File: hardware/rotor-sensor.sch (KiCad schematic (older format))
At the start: 26 parts, among them J1 Conn_01x03, J2 Conn_01x03, J3 Conn_01x03, U1 ATtiny202-SS, U2 EE-SX1081, U3 SM351LT

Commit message: Second hardware iteration (#3)
Cleaned up the schematic and reworked the entire PCB.
Replaced EE-SX1083 with EE-SX199, added 3D model and new component.
Added modified worksheet so that the PCB origin can be 0, 0.
Added scripts to execute certain tasks locally and updated the workflow accordingly.
Workflow now runs for the different variants.
The KiBot configuration has been merged into a single file.
*Increased clearance between Slot sensor and PCB edge
Assigned component values to remaining components.
Connectors will now only be placed in the DEBUG variant
Rotated input filter capacitor for better ground connection
Adds panelization and panel configuration
Adds fiducials to board and added tab annotation as a footprint.
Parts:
- removed TP1, TP2, TP3, TP4, TP5, TP6: TestPoint_Alt, TestPoint:TestPoint_Pad_D1.0mm, symbol Connector:TestPoint_Alt
- removed U2: EE-SX1081, local:EE-SX1081, symbol local:EE-SX1081
- added FID1, FID2: Fiducial, Fiducial:Fiducial_0.5mm_Mask1.5mm, symbol Mechanical:Fiducial
- added TP1: +, TestPoint:TestPoint_Pad_D1.0mm, symbol Connector:TestPoint_Small
- added TP10: AC-, TestPoint:TestPoint_Pad_D1.0mm, symbol Connector:TestPoint_Small
- added TP11: AC+, TestPoint:TestPoint_Pad_D1.0mm, symbol Connector:TestPoint_Small
- added TP12: IN, TestPoint:TestPoint_Pad_D1.0mm, symbol Connector:TestPoint_Small
- added TP13: OUT, TestPoint:TestPoint_Pad_D1.0mm, symbol Connector:TestPoint_Small
- added TP2: COMA, TestPoint:TestPoint_Pad_D1.0mm, symbol Connector:TestPoint_Small
- added TP3: VD, TestPoint:TestPoint_Pad_D1.0mm, symbol Connector:TestPoint_Small
- added TP4: VCC, TestPoint:TestPoint_Pad_D1.0mm, symbol Connector:TestPoint_Small
- added TP5: -, TestPoint:TestPoint_Pad_D1.0mm, symbol Connector:TestPoint_Small
- added TP6: UPDI, TestPoint:TestPoint_Pad_D1.0mm, symbol Connector:TestPoint_Small
- added TP7: COMB, TestPoint:TestPoint_Pad_D1.0mm, symbol Connector:TestPoint_Small
- added TP8: W2, TestPoint:TestPoint_Pad_D1.0mm, symbol Connector:TestPoint_Small
- added TP9: SENSE, TestPoint:TestPoint_Pad_D1.0mm, symbol Connector:TestPoint_Small
- added U2: EE-SX199, local:EE-SX199, symbol local:EE-SX199
- C1, C2, C3: value C -> 100n
- J1, J2, J3: Config (none) -> +DEBUG
- L1: value L -> 10uH
- R1, R4, R5: value R -> 50m
- R2: value R -> 1k
- R3: value R -> 100
- R6, R7: value R -> 1k; Config (none) -> +IREF
- U3: Config (none) -> +HALL
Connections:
- net labels added: OS_INPUT, OS_OUTPUT, PA0_UPDI
- wire segments 60 -> 68
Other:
- note added: "EXTERNAL SENSOR\nCONNECTOR"
- note added: "EXTERNAL VOLTAGE\nREFERENCE"
- note added: "ONBOARD\nHALL SENSOR"
- note added: "ONBOARD\nOPTICAL SENSOR"
- note added: "VARIANT=EXTERNAL"
- note added: "VARIANT=HALL"
- note added: "VARIANT=IREF"
- note added: "VARIANT=OPTICAL"
- note removed: "ONBOARD PERIPHERALS"
- moved on the sheet: C1, C2, C3, D1, D2, D3, J1, J2, J3, L1, R1, R2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

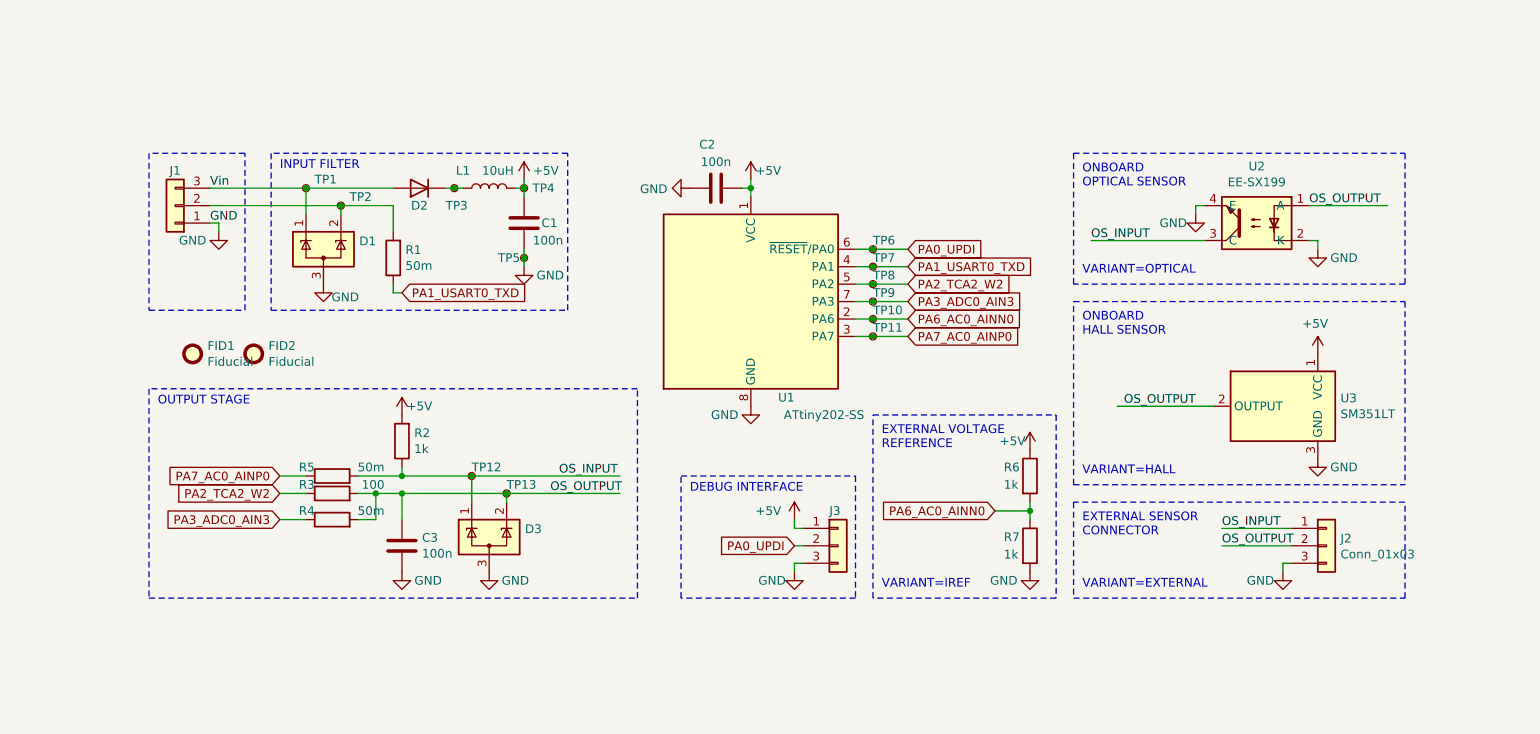
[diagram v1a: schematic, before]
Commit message: Adds LIN Transceiver to the design
Updates layout and schematic
Adds overcurrent protection IC and removes sense line
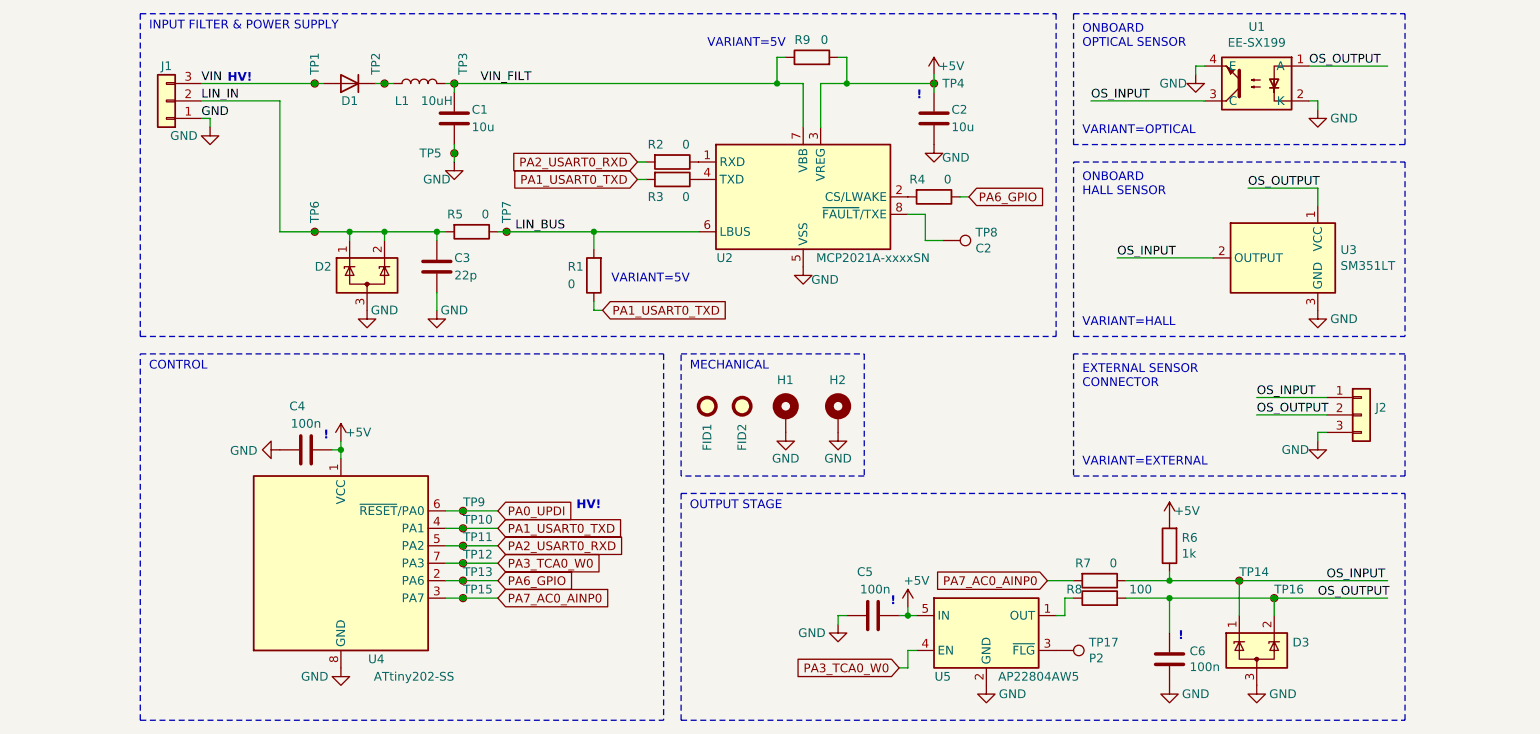
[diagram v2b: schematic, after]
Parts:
- removed J3: Conn_01x03, Connector_PinHeader_1.27mm:PinHeader_1x03_P1.27mm_Vertical, symbol Connector_Generic:Conn_01x03
- removed R5: 50m, Resistor_SMD:R_0603_1608Metric, symbol Device:R
- removed R6: 1k, Resistor_SMD:R_0603_1608Metric, symbol Device:R
- added C2: 10u, Capacitor_SMD:C_1206_3216Metric, symbol Device:C
- added C3: 22p, Capacitor_SMD:C_0603_1608Metric, symbol Device:C
- added C5: 100n, Capacitor_SMD:C_0603_1608Metric, symbol Device:C
- added H1, H2: MountingHole_Pad, MountingHole:MountingHole_2.2mm_M2_DIN965_Pad_TopOnly, symbol Mechanical:MountingHole_Pad
- added R1, R2, R3: 0, Resistor_SMD:R_0402_1005Metric, symbol Device:R
- added R9: 0, Resistor_SMD:R_0603_1608Metric, symbol Device:R
- added TP17: P2, TestPoint:TestPoint_Pad_D1.0mm, symbol Connector:TestPoint
- added TP4: V3, TestPoint:TestPoint_Pad_D1.0mm, symbol Connector:TestPoint_Small
- added TP7: C1, TestPoint:TestPoint_Pad_D1.0mm, symbol Connector:TestPoint_Small
- added TP8: C2, TestPoint:TestPoint_Pad_D1.0mm, symbol Connector:TestPoint
- added U2: MCP2021A-xxxxSN, Package_SO:SOIC-8_3.9x4.9mm_P1.27mm, symbol Interface_CAN_LIN:MCP2021A-xxxxSN
- added U5: AP22804AW5, Package_TO_SOT_SMD:SOT-23-5, symbol Power_Management:AP22804AW5
- C1: value 100n -> 10u; footprint Capacitor_SMD:C_0603_1608Metric -> Capacitor_SMD:C_1206_3216Metric
- J1: footprint Connector_PinHeader_2.54mm:PinHeader_1x03_P2.54mm_Vertical -> Connector_JST:JST_PH_B3B-PH-K_1x03_P2.00mm_Vertical
- R4: value 50m -> 0; footprint Resistor_SMD:R_0603_1608Metric -> Resistor_SMD:R_0402_1005Metric
- R5: renamed from R1; value 50m -> 0; footprint Resistor_SMD:R_0603_1608Metric -> Resistor_SMD:R_0402_1005Metric
- R7: value 1k -> 0; footprint Resistor_SMD:R_0603_1608Metric -> Resistor_SMD:R_0402_1005Metric; Config +IREF -> (none)
- TP1: value + -> V0
- TP10: renamed from TP7; value COMB -> M1
- TP11: renamed from TP8; value W2 -> M2
- TP12: renamed from TP9; value SENSE -> M3
- TP13: renamed from TP10; value AC- -> M6
- TP14: renamed from TP12; value IN -> P0
- TP15: renamed from TP11; value AC+ -> M7
- TP16: renamed from TP13; value OUT -> P1
- TP2: value COMA -> V1
- TP3: renamed from TP4; value VCC -> V2
- TP5: value - -> V4
- TP6: renamed from TP3; value VD -> C0
- TP9: renamed from TP6; value UPDI -> M0
- renumbered C2 to C4, C3 to C6, D2 to D1, D1 to D2, FID2 to FID1, FID1 to FID2, R2 to R6, R3 to R8, U2 to U1, U1 to U4
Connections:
- net labels added: LIN_BUS, LIN_IN, PA2_USART0_RXD, PA3_TCA0_W0, PA6_GPIO, VIN, VIN_FILT
- net labels removed: PA2_TCA2_W2, PA3_ADC0_AIN3, PA6_AC0_AINN0, Vin
- wire segments 68 -> 95
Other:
- note added: "!"
- note added: "CONTROL"
- note added: "HV!"
- note added: "INPUT FILTER & POWER SUPPLY"
- note added: "MECHANICAL"
- note added: "VARIANT=5V"
- note removed: "DEBUG INTERFACE"
- note removed: "EXTERNAL VOLTAGE\nREFERENCE"
- note removed: "INPUT FILTER"
- note removed: "VARIANT=IREF"
- moved on the sheet: C1, C4, C6, D1, D2, D3, FID1, FID2, J1, J2, L1, R5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

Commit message: Panelize?
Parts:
- added D4: LED_Small, LED_SMD:LED_0603_1608Metric, symbol Device:LED_Small
- added R10: 220, Resistor_SMD:R_0603_1608Metric, symbol Device:R
- R1, R9: Config (none) -> +5V
- U2: Config (none) -> -5V
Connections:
- wire segments 95 -> 100
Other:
- note added: "VARIANT=12V"
- moved on the sheet: C5, C6, D3, R7, R8, TP17, U5
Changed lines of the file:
@@
 L Device:R R8
 U 1 1 6122E61F
-P 7800 5100
-F 0 "R8" V 7850 5200 50  0000 L CNN
-F 1 "100" V 7850 4800 50  0000 L CNN
-F 2 "Resistor_SMD:R_0603_1608Metric" V 7730 5100 50  0001 C CNN
-F 3 "~" H 7800 5100 50  0001 C CNN
-	1    7800 5100
+P 7450 5100
+F 0 "R8" V 7500 5200 50  0000 L CNN
+F 1 "100" V 7500 4800 50  0000 L CNN
+F 2 "Resistor_SMD:R_0603_1608Metric" V 7380 5100 50  0001 C CNN
+F 3 "~" H 7450 5100 50  0001 C CNN
+	1    7450 5100
 	0    -1   -1   0
 $EndComp
@@
 	-1   0    0    1
 $EndComp
-Text GLabel 7500 5000 0    50   Input ~ 0
+Text GLabel 7150 5000 0    50   Input ~ 0
 PA7_AC0_AINP0
 Wire Wire Line
-	7600 5100 7650 5100
+	7250 5100 7300 5100
 Text GLabel 4350 4700 2    50   Input ~ 0
 PA1_USART0_TXD
@@
 L Power_Protection:SP0502BAHT D3
 U 1 1 613650DD
-P 8700 5400
-F 0 "D3" H 8905 5446 50  0000 L CNN
-F 1 "SP0502BAHT" H 8900 5350 50  0001 L CNN
-F 2 "Package_TO_SOT_SMD:SOT-23" H 8925 5350 50  0001 L CNN
-F 3 "http://www.littelfuse.com/~/media/files/littelfuse/technical%20resources/documents/data%20sheets/sp05xxba.pdf" H 8825 5525 50  0001 C CNN
-	1    8700 5400
+P 8700 5450
+F 0 "D3" H 8905 5496 50  0000 L CNN
+F 1 "SP0502BAHT" H 8900 5400 50  0001 L CNN
+F 2 "Package_TO_SOT_SMD:SOT-23" H 8925 5400 50  0001 L CNN
+F 3 "http://www.littelfuse.com/~/media/files/littelfuse/technical%20resources/documents/data%20sheets/sp05xxba.pdf" H 8825 5575 50  0001 C CNN
+	1    8700 5450
 	1    0    0    -1
 $EndComp
@@
 	8200 4950 8200 5000
 Wire Wire Line
-	8200 5300 8200 5100
+	8200 5350 8200 5100
 $Comp
 L power:GND #PWR024
 U 1 1 613B542D
-P 8700 5600
-F 0 "#PWR024" H 8700 5350 50  0001 C CNN
-F 1 "GND" H 8850 5550 50  0000 C CNN
-F 2 "" H 8700 5600 50  0001 C CNN
-F 3 "" H 8700 5600 50  0001 C CNN
-	1    8700 5600
+P 8700 5650
+F 0 "#PWR024" H 8700 5400 50  0001 C CNN
+F 1 "GND" H 8850 5600 50  0000 C CNN
+F 2 "" H 8700 5650 50  0001 C CNN
+F 3 "" H 8700 5650 50  0001 C CNN
+	1    8700 5650
 	1    0    0    -1
 $EndComp
@@
 L power:GND #PWR023
 U 1 1 6127F551
-P 8200 5600
-F 0 "#PWR023" H 8200 5350 50  0001 C CNN
-F 1 "GND" H 8350 5550 50  0000 C CNN
-F 2 "" H 8200 5600 50  0001 C CNN
-F 3 "" H 8200 5600 50  0001 C CNN
-	1    8200 5600
+P 8200 5650
+F 0 "#PWR023" H 8200 5400 50  0001 C CNN
+F 1 "GND" H 8350 5600 50  0000 C CNN
+F 2 "" H 8200 5650 50  0001 C CNN
+F 3 "" H 8200 5650 50  0001 C CNN
+	1    8200 5650
 	1    0    0    -1
 $EndComp
@@
 L Device:C C6
 U 1 1 61263E24
-P 8200 5450
-F 0 "C6" H 8315 5496 50  0000 L CNN
-F 1 "100n" H 8315 5405 50  0000 L CNN
-F 2 "Capacitor_SMD:C_0603_1608Metric" H 8238 5300 50  0001 C CNN
-F 3 "~" H 8200 5450 50  0001 C CNN
-	1    8200 5450
+P 8200 5500
+F 0 "C6" H 8315 5546 50  0000 L CNN
+F 1 "100n" H 8315 5455 50  0000 L CNN
+F 2 "Capacitor_SMD:C_0603_1608Metric" H 8238 5350 50  0001 C CNN
+F 3 "~" H 8200 5500 50  0001 C CNN
+	1    8200 5500
 	1    0    0    -1
 $EndComp
@@
 OUTPUT STAGE
 Wire Wire Line
-	8200 5000 7950 5000
-Wire Wire Line
-	7650 5000 7500 5000
+	8200 5000 7600 5000
+Wire Wire Line
+	7300 5000 7150 5000
 Text GLabel 4350 4600 2    50   Input ~ 0
 PA0_UPDI
@@
 	8350 2050 8400 2050
 Wire Wire Line
-	8800 5200 8800 5100
+	8800 5250 8800 5100
 Connection ~ 8800 5100
 Wire Wire Line
-	8600 5200 8600 5000
+	8600 5250 8600 5000
 Connection ~ 8600 5000
 Wire Wire Line
@@
 F 2 "Package_SO:SOIC-8_3.9x4.9mm_P1.27mm" H 6125 2875 50  0001 C CNN
 F 3 "http://ww1.microchip.com/downloads/en/DeviceDoc/20002298C.pdf" H 6125 2875 50  0001 C CNN
+F 4 "-5V" H 6100 2800 50  0001 C CNN "Config"
 	1    6100 2800
 	1    0    0    -1
@@
 Text GLabel 4350 4800 2    50   Input ~ 0
 PA2_USART0_RXD
-Wire Wire Line
-	7950 5100 8200 5100
 $Comp
 L Power_Management:AP22804AW5 U5
 U 1 1 623B800F
-P 7150 5300
-F 0 "U5" H 6900 5050 50  0000 C CNN
-F 1 "AP22804AW5" H 7450 5050 50  0000 C CNN
-F 2 "Package_TO_SOT_SMD:SOT-23-5" H 7150 4900 50  0001 C CNN
-F 3 "https://www.diodes.com/assets/Datasheets/AP22804_14.pdf" H 7150 5350 50  0001 C CNN
-	1    7150 5300
+P 6800 5300
+F 0 "U5" H 6550 5050 50  0000 C CNN
+F 1 "AP22804AW5" H 7100 5050 50  0000 C CNN
+F 2 "Package_TO_SOT_SMD:SOT-23-5" H 6800 4900 50  0001 C CNN
+F 3 "https://www.diodes.com/assets/Datasheets/AP22804_14.pdf" H 6800 5350 50  0001 C CNN
+	1    6800 5300
 	1    0    0    -1
 $EndComp
@@
 	5150 2700 5200 2700
 Wire Wire Line
-	7550 5200 7600 5200
-Wire Wire Line
-	7600 5200 7600 5100
+	7200 5200 7250 5200
+Wire Wire Line
+	7250 5200 7250 5100
 Text GLabel 4350 4900 2    50   Input ~ 0
 PA3_TCA0_W0
 Text GLabel 4350 5000 2    50   Input ~ 0
 PA6_GPIO
-Text GLabel 6650 5500 0    50   Input ~ 0
+Text GLabel 6300 5500 0    50   Input ~ 0
 PA3_TCA0_W0
 $Comp
 L power:+5V #PWR019
 U 1 1 623E7E3D
-P 6700 5150
-F 0 "#PWR019" H 6700 5000 50  0001 C CNN
-F 1 "+5V" H 6750 5300 50  0000 C CNN
-F 2 "" H 6700 5150 50  0001 C CNN
-F 3 "" H 6700 5150 50  0001 C CNN
-	1    6700 5150
-	1    0    0    -1
-$EndComp
-Wire Wire Line
-	6700 5400 6750 5400
-Wire Wire Line
-	6700 5150 6700 5200
-Wire Wire Line
-	6700 5200 6750 5200
+P 6350 5150
+F 0 "#PWR019" H 6350 5000 50  0001 C CNN
+F 1 "+5V" H 6400 5300 50  0000 C CNN
+F 2 "" H 6350 5150 50  0001 C CNN
+F 3 "" H 6350 5150 50  0001 C CNN
+	1    6350 5150
+	1    0    0    -1
+$EndComp
+Wire Wire Line
+	6350 5400 6400 5400
+Wire Wire Line
+	6350 5150 6350 5200
+Wire Wire Line
+	6350 5200 6400 5200
 $Comp
 L power:GND #PWR022
 U 1 1 623F4191
-P 7150 5600
-F 0 "#PWR022" H 7150 5350 50  0001 C CNN
-F 1 "GND" H 7300 5550 50  0000 C CNN
-F 2 "" H 7150 5600 50  0001 C CNN
-F 3 "" H 7150 5600 50  0001 C CNN
-	1    7150 5600
+P 6800 5600
+F 0 "#PWR022" H 6800 5350 50  0001 C CNN
+F 1 "GND" H 6950 5550 50  0000 C CNN
+F 2 "" H 6800 5600 50  0001 C CNN
+F 3 "" H 6800 5600 50  0001 C CNN
+	1    6800 5600
 	1    0    0    -1
 $EndComp
@@
 L Device:C C5
 U 1 1 623F6E9E
-P 6500 5200
-F 0 "C5" V 6750 5200 50  0000 L CNN
-F 1 "100n" V 6650 5100 50  0000 L CNN
-F 2 "Capacitor_SMD:C_0603_1608Metric" H 6538 5050 50  0001 C CNN
-F 3 "~" H 6500 5200 50  0001 C CNN
-	1    6500 5200
+P 6150 5200
+F 0 "C5" V 6400 5200 50  0000 L CNN
+F 1 "100n" V 6300 5100 50  0000 L CNN
+F 2 "Capacitor_SMD:C_0603_1608Metric" H 6188 5050 50  0001 C CNN
+F 3 "~" H 6150 5200 50  0001 C CNN
+	1    6150 5200
 	0    -1   -1   0
 $EndComp
@@
 L power:GND #PWR020
 U 1 1 6248AFD5
-P 6300 5250
-F 0 "#PWR020" H 6300 5000 50  0001 C CNN
-F 1 "GND" H 6150 5200 50  0000 C CNN
-F 2 "" H 6300 5250 50  0001 C CNN
-F 3 "" H 6300 5250 50  0001 C CNN
-	1    6300 5250
-	1    0    0    -1
-$EndComp
-Wire Wire Line
-	6650 5500 6700 5500
-Wire Wire Line
-	6700 5500 6700 5400
-Wire Wire Line
-	6300 5250 6300 5200
+P 5950 5250
+F 0 "#PWR020" H 5950 5000 50  0001 C CNN
+F 1 "GND" H 5800 5200 50  0000 C CNN
+F 2 "" H 5950 5250 50  0001 C CNN
+F 3 "" H 5950 5250 50  0001 C CNN
+	1    5950 5250
+	1    0    0    -1
+$EndComp
+Wire Wire Line
+	6300 5500 6350 5500
+Wire Wire Line
+	6350 5500 6350 5400
+Wire Wire Line
+	5950 5250 5950 5200
+Wire Wire Line
+	5950 5200 6000 5200
 Wire Wire Line
 	6300 5200 6350 5200
-Wire Wire Line
-	6650 5200 6700 5200
-Connection ~ 6700 5200
+Connection ~ 6350 5200
 Wire Notes Line
 	5400 4500 9550 4500
@@
 L Device:R R7
 U 1 1 6258FF8B
-P 7800 5000
-F 0 "R7" V 7700 4950 50  0000 R CNN
-F 1 "0" V 7700 5100 50  0000 R CNN
-F 2 "Resistor_SMD:R_0402_1005Metric" V 7730 5000 50  0001 C CNN
-F 3 "~" H 7800 5000 50  0001 C CNN
-	1    7800 5000
+P 7450 5000
+F 0 "R7" V 7350 4950 50  0000 R CNN
+F 1 "0" V 7350 5100 50  0000 R CNN
+F 2 "Resistor_SMD:R_0402_1005Metric" V 7380 5000 50  0001 C CNN
+F 3 "~" H 7450 5000 50  0001 C CNN
+	1    7450 5000
 	0    1    1    0
 $EndComp
@@
 L Connector:TestPoint TP17
 U 1 1 626156D9
-P 7550 5400
-F 0 "TP17" V 7504 5588 50  0000 L CNN
-F 1 "P2" V 7595 5588 50  0000 L CNN
-F 2 "TestPoint:TestPoint_Pad_D1.0mm" H 7750 5400 50  0001 C CNN
-F 3 "~" H 7750 5400 50  0001 C CNN
-	1    7550 5400
+P 7200 5400
+F 0 "TP17" V 7250 5600 50  0000 L CNN
+F 1 "P2" V 7300 5600 50  0001 L CNN
+F 2 "TestPoint:TestPoint_Pad_D1.0mm" H 7400 5400 50  0001 C CNN
+F 3 "~" H 7400 5400 50  0001 C CNN
+	1    7200 5400
 	0    1    1    0
 $EndComp
@@
 Text Label 8650 2750 0    50   ~ 0
 OS_OUTPUT
-Text Notes 6600 5150 0    50   ~ 10
+Text Notes 6250 5150 0    50   ~ 10
 !
 Text Notes 6750 2250 0    50   ~ 10
@@
 F 2 "Resistor_SMD:R_0402_1005Metric" V 4830 3250 50  0001 C CNN
 F 3 "~" H 4900 3250 50  0001 C CNN
+F 4 "+5V" H 4900 3250 50  0001 C CNN "Config"
 	1    4900 3250
 	-1   0    0    1
@@
 F 2 "Resistor_SMD:R_0603_1608Metric" V 6080 2000 50  0001 C CNN
 F 3 "~" H 6150 2000 50  0001 C CNN
+F 4 "+5V" V 6150 2000 50  0001 C CNN "Config"
 	1    6150 2000
 	0    -1   -1   0
@@
 Text Notes 5000 3300 0    50   ~ 0
 VARIANT=5V
+$Comp
+L Device:R R10
+U 1 1 6253E802
+P 7450 5300
+F 0 "R10" V 7400 5100 50  0000 L CNN
+F 1 "220" V 7400 5450 50  0000 L CNN
+F 2 "Resistor_SMD:R_0603_1608Metric" V 7380 5300 50  0001 C CNN
+F 3 "~" H 7450 5300 50  0001 C CNN
+	1    7450 5300
+	0    1    1    0
+$EndComp
+$Comp
+L Device:LED_Small D4
+U 1 1 6253FA73
+P 7850 5300
+F 0 "D4" H 7900 5200 50  0000 R CNN
+F 1 "LED_Small" V 7800 5500 50  0001 R CNN
+F 2 "LED_SMD:LED_0603_1608Metric" V 7850 5300 50  0001 C CNN
+F 3 "~" V 7850 5300 50  0001 C CNN
+	1    7850 5300
+	-1   0    0    1
+$EndComp
+$Comp
+L power:GND #PWR0101
+U 1 1 625403F5
+P 8000 5350
+F 0 "#PWR0101" H 8000 5100 50  0001 C CNN
+F 1 "GND" H 7900 5250 50  0000 C CNN
+F 2 "" H 8000 5350 50  0001 C CNN
+F 3 "" H 8000 5350 50  0001 C CNN
+	1    8000 5350
+	1    0    0    -1
+$EndComp
+Wire Wire Line
+	7600 5100 8200 5100
+Wire Wire Line
+	7250 5200 7250 5300
+Wire Wire Line
+	7250 5300 7300 5300
+Connection ~ 7250 5200
+Wire Wire Line
+	7950 5300 8000 5300
+Wire Wire Line
+	8000 5300 8000 5350
+Wire Wire Line
+	7600 5300 7750 5300
+Text Notes 5550 2450 0    50   ~ 0
+VARIANT=12V
 $EndSCHEMATC
